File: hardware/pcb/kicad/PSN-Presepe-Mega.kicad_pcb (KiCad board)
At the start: 2 copper layers, 280 x 170 mm, 77 parts, among them J1 12V_IN, K1 G5Q-1_DC12, K10 G5Q-1_DC12, K11 G5Q-1_DC12, K12 G5Q-1_DC12, K13 G5Q-1_DC12, K14 G5Q-1_DC12, K15 G5Q-1_DC12, K16 G5Q-1_DC12, K2 G5Q-1_DC12, K3 G5Q-1_DC12, K4 G5Q-1_DC12, K5 G5Q-1_DC12, K6 G5Q-1_DC12, K7 G5Q-1_DC12, K8 G5Q-1_DC12, K9 G5Q-1_DC12, Q1 IRLZ44N_CIELO_R, Q2 IRLZ44N_CIELO_G, Q3 IRLZ44N_CIELO_B, Q4 IRLZ44N_TRAM_R, Q5 IRLZ44N_TRAM_G, Q6 IRLZ44N_TRAM_B, Q7 IRLZ44N_ALBA_R, Q8 IRLZ44N_ALBA_G, Q9 IRLZ44N_ALBA_B, U1 ULN2803C, U2 ULN2803C

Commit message: Increase right-edge relay terminal board margins
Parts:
- moved JR16 14.0 mm to (292.0, 160.0)
- moved JR15 13.0 mm to (292.0, 144.0)
- moved JR14 12.0 mm to (292.0, 128.0)
- moved JR13 11.0 mm to (292.0, 112.0)
- moved JR12 10.0 mm to (292.0, 96.0)
- moved JR11 9.00 mm to (292.0, 80.0)
- moved JR10 8.00 mm to (292.0, 64.0)
- moved JR9 7.00 mm to (292.0, 48.0)
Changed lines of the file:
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@@
       (pad "3" thru_hole circle (at 10.16 0 90) (size 2.6 2.6) (drill 1.3) (layers "*.Cu" "*.Mask") (net 93 "R8_NC"))
     )
-  (footprint "PSN_Presep_Custom:TerminalBlock_Phoenix_MKDS-1.5-3-5.08" (layer "F.Cu") (at 292 55 90)
+  (footprint "PSN_Presep_Custom:TerminalBlock_Phoenix_MKDS-1.5-3-5.08" (layer "F.Cu") (at 292 48 90)
       (property "Reference" "JR9" (at 5.08 -3 90) (layer "F.SilkS") (effects (font (size 0.9 0.9) (thickness 0.15))))
       (property "Value" "COM_NO_NC" (at 5.08 3 90) (layer "F.Fab") (effects (font (size 0.8 0.8) (thickness 0.12))))
@@
       (pad "3" thru_hole circle (at 10.16 0 90) (size 2.6 2.6) (drill 1.3) (layers "*.Cu" "*.Mask") (net 96 "R9_NC"))
     )
-  (footprint "PSN_Presep_Custom:TerminalBlock_Phoenix_MKDS-1.5-3-5.08" (layer "F.Cu") (at 292 72 90)
+  (footprint "PSN_Presep_Custom:TerminalBlock_Phoenix_MKDS-1.5-3-5.08" (layer "F.Cu") (at 292 64 90)
       (property "Reference" "JR10" (at 5.08 -3 90) (layer "F.SilkS") (effects (font (size 0.9 0.9) (thickness 0.15))))
       (property "Value" "COM_NO_NC" (at 5.08 3 90) (layer "F.Fab") (effects (font (size 0.8 0.8) (thickness 0.12))))
@@
       (pad "3" thru_hole circle (at 10.16 0 90) (size 2.6 2.6) (drill 1.3) (layers "*.Cu" "*.Mask") (net 99 "R10_NC"))
     )
-  (footprint "PSN_Presep_Custom:TerminalBlock_Phoenix_MKDS-1.5-3-5.08" (layer "F.Cu") (at 292 89 90)
+  (footprint "PSN_Presep_Custom:TerminalBlock_Phoenix_MKDS-1.5-3-5.08" (layer "F.Cu") (at 292 80 90)
       (property "Reference" "JR11" (at 5.08 -3 90) (layer "F.SilkS") (effects (font (size 0.9 0.9) (thickness 0.15))))
       (property "Value" "COM_NO_NC" (at 5.08 3 90) (layer "F.Fab") (effects (font (size 0.8 0.8) (thickness 0.12))))
@@
       (pad "3" thru_hole circle (at 10.16 0 90) (size 2.6 2.6) (drill 1.3) (layers "*.Cu" "*.Mask") (net 102 "R11_NC"))
     )
-  (footprint "PSN_Presep_Custom:TerminalBlock_Phoenix_MKDS-1.5-3-5.08" (layer "F.Cu") (at 292 106 90)
+  (footprint "PSN_Presep_Custom:TerminalBlock_Phoenix_MKDS-1.5-3-5.08" (layer "F.Cu") (at 292 96 90)
       (property "Reference" "JR12" (at 5.08 -3 90) (layer "F.SilkS") (effects (font (size 0.9 0.9) (thickness 0.15))))
       (property "Value" "COM_NO_NC" (at 5.08 3 90) (layer "F.Fab") (effects (font (size 0.8 0.8) (thickness 0.12))))
@@
       (pad "3" thru_hole circle (at 10.16 0 90) (size 2.6 2.6) (drill 1.3) (layers "*.Cu" "*.Mask") (net 105 "R12_NC"))
     )
-  (footprint "PSN_Presep_Custom:TerminalBlock_Phoenix_MKDS-1.5-3-5.08" (layer "F.Cu") (at 292 123 90)
+  (footprint "PSN_Presep_Custom:TerminalBlock_Phoenix_MKDS-1.5-3-5.08" (layer "F.Cu") (at 292 112 90)
       (property "Reference" "JR13" (at 5.08 -3 90) (layer "F.SilkS") (effects (font (size 0.9 0.9) (thickness 0.15))))
       (property "Value" "COM_NO_NC" (at 5.08 3 90) (layer "F.Fab") (effects (font (size 0.8 0.8) (thickness 0.12))))
@@
       (pad "3" thru_hole circle (at 10.16 0 90) (size 2.6 2.6) (drill 1.3) (layers "*.Cu" "*.Mask") (net 108 "R13_NC"))
     )
-  (footprint "PSN_Presep_Custom:TerminalBlock_Phoenix_MKDS-1.5-3-5.08" (layer "F.Cu") (at 292 140 90)
+  (footprint "PSN_Presep_Custom:TerminalBlock_Phoenix_MKDS-1.5-3-5.08" (layer "F.Cu") (at 292 128 90)
       (property "Reference" "JR14" (at 5.08 -3 90) (layer "F.SilkS") (effects (font (size 0.9 0.9) (thickness 0.15))))
       (property "Value" "COM_NO_NC" (at 5.08 3 90) (layer "F.Fab") (effects (font (size 0.8 0.8) (thickness 0.12))))
@@
       (pad "3" thru_hole circle (at 10.16 0 90) (size 2.6 2.6) (drill 1.3) (layers "*.Cu" "*.Mask") (net 111 "R14_NC"))
     )
-  (footprint "PSN_Presep_Custom:TerminalBlock_Phoenix_MKDS-1.5-3-5.08" (layer "F.Cu") (at 292 157 90)
+  (footprint "PSN_Presep_Custom:TerminalBlock_Phoenix_MKDS-1.5-3-5.08" (layer "F.Cu") (at 292 144 90)
       (property "Reference" "JR15" (at 5.08 -3 90) (layer "F.SilkS") (effects (font (size 0.9 0.9) (thickness 0.15))))
       (property "Value" "COM_NO_NC" (at 5.08 3 90) (layer "F.Fab") (effects (font (size 0.8 0.8) (thickness 0.12))))
@@
       (pad "3" thru_hole circle (at 10.16 0 90) (size 2.6 2.6) (drill 1.3) (layers "*.Cu" "*.Mask") (net 114 "R15_NC"))
     )
-  (footprint "PSN_Presep_Custom:TerminalBlock_Phoenix_MKDS-1.5-3-5.08" (layer "F.Cu") (at 292 174 90)
+  (footprint "PSN_Presep_Custom:TerminalBlock_Phoenix_MKDS-1.5-3-5.08" (layer "F.Cu") (at 292 160 90)
       (property "Reference" "JR16" (at 5.08 -3 90) (layer "F.SilkS") (effects (font (size 0.9 0.9) (thickness 0.15))))
       (property "Value" "COM_NO_NC" (at 5.08 3 90) (layer "F.Fab") (effects (font (size 0.8 0.8) (thickness 0.12))))

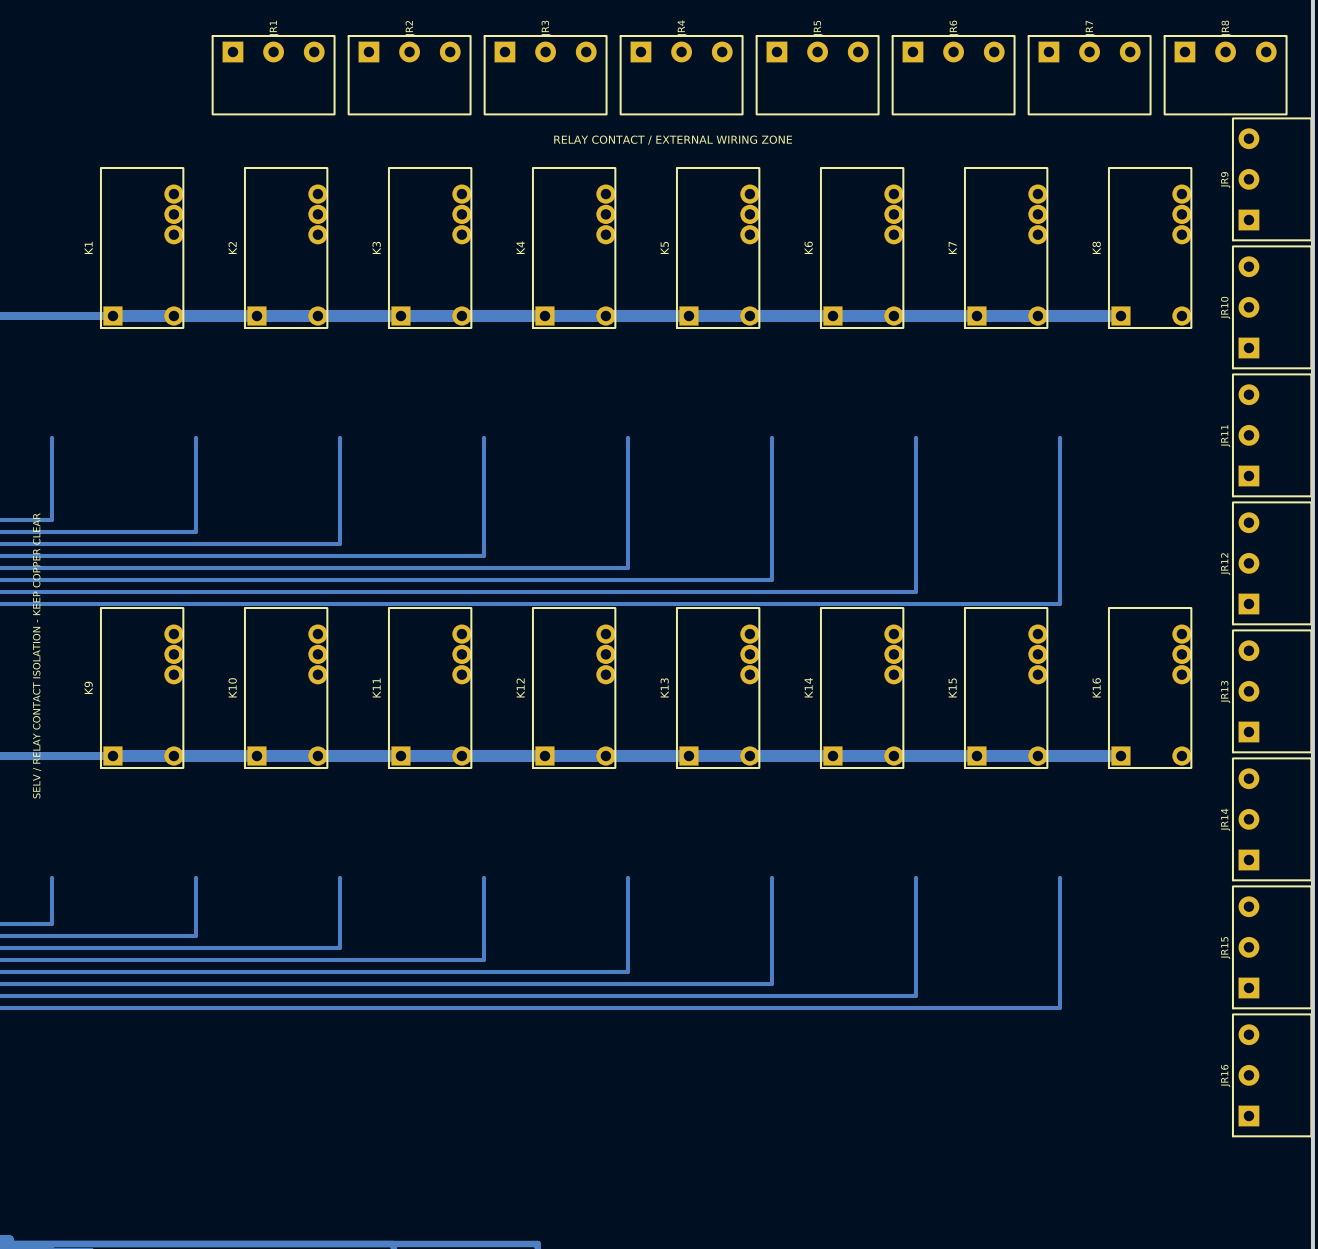
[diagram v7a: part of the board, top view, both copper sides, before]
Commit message: Route isolated relay COM NO NC contact networks
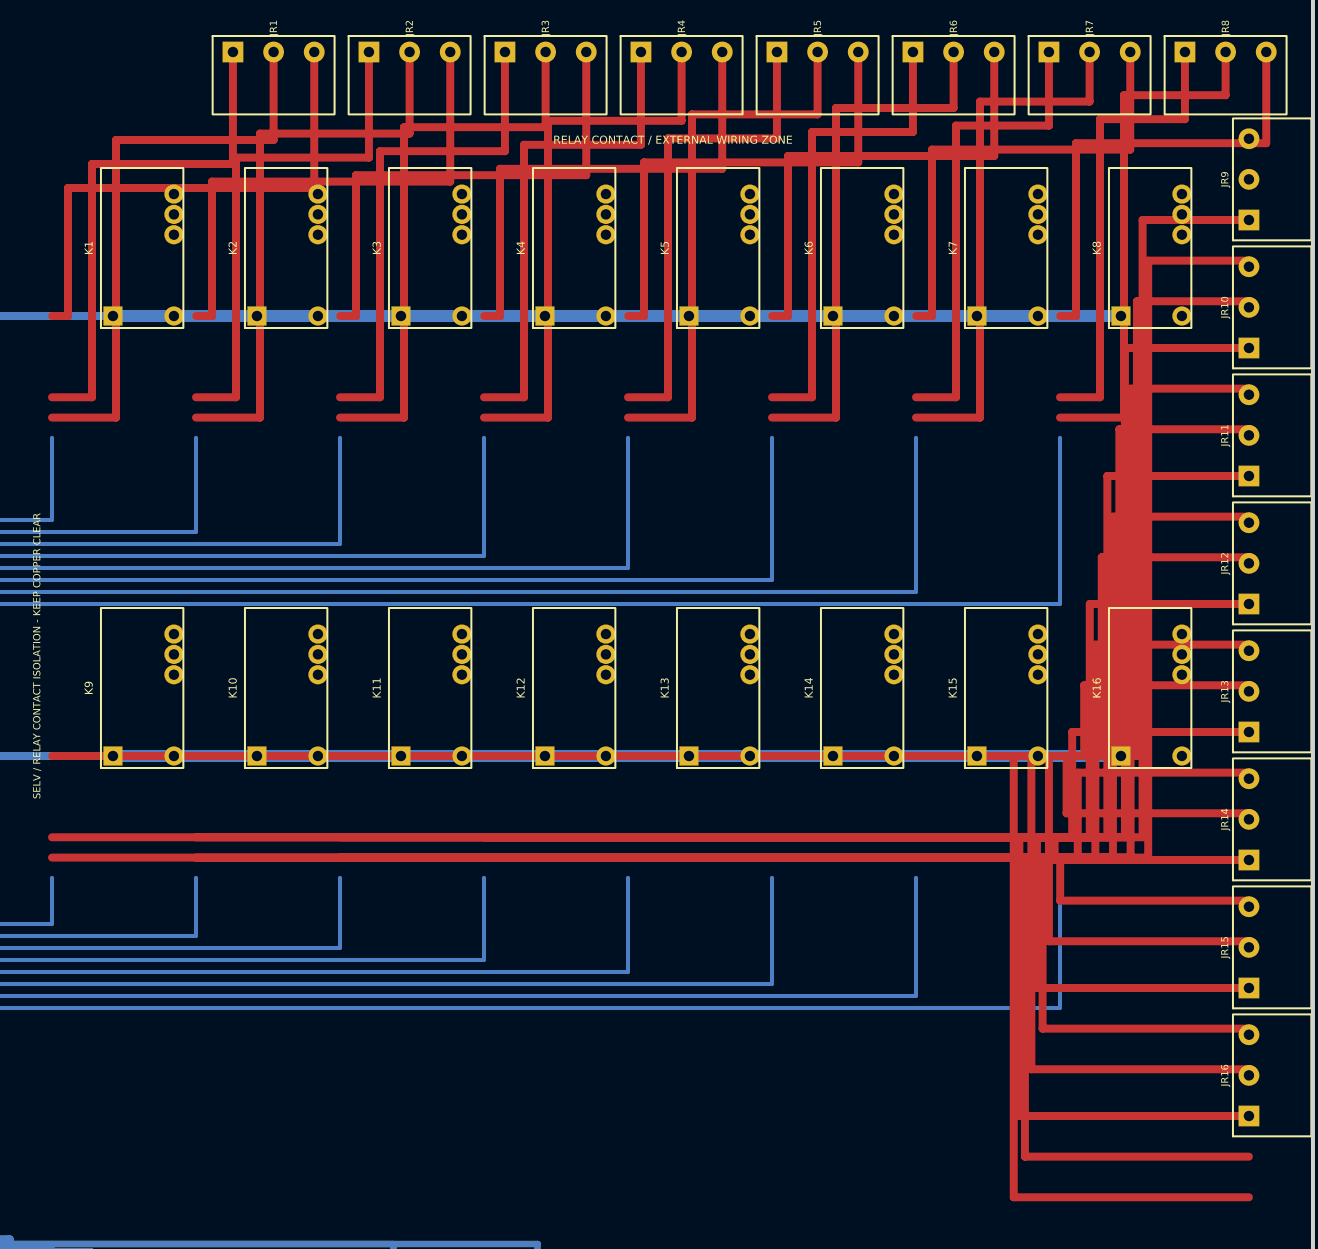
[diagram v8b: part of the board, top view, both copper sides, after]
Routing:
- net R9_COM: track 0.00 -> 226.8 mm
- net R9_NO: track 0.00 -> 224.2 mm
- net R9_NC: track 0.00 -> 206.5 mm
- net R10_COM: track 0.00 -> 192.8 mm
- net R10_NO: track 0.00 -> 190.2 mm
- net R10_NC: track 0.00 -> 172.5 mm
- net R11_COM: track 0.00 -> 158.8 mm
- net R11_NO: track 0.00 -> 156.2 mm
- net R11_NC: track 0.00 -> 138.5 mm
- net R12_COM: track 0.00 -> 124.8 mm
- net R12_NO: track 0.00 -> 122.2 mm
- net R12_NC: track 0.00 -> 104.5 mm
- net R13_COM: track 0.00 -> 90.8 mm
- net R16_NC: track 0.00 -> 90.3 mm
- net R13_NO: track 0.00 -> 88.2 mm
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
